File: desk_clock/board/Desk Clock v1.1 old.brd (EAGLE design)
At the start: 79 x 35.9 mm, 17 parts, among them IC1 PIC16F628P, IC2 MAX7219CNG, U1 TMP75D

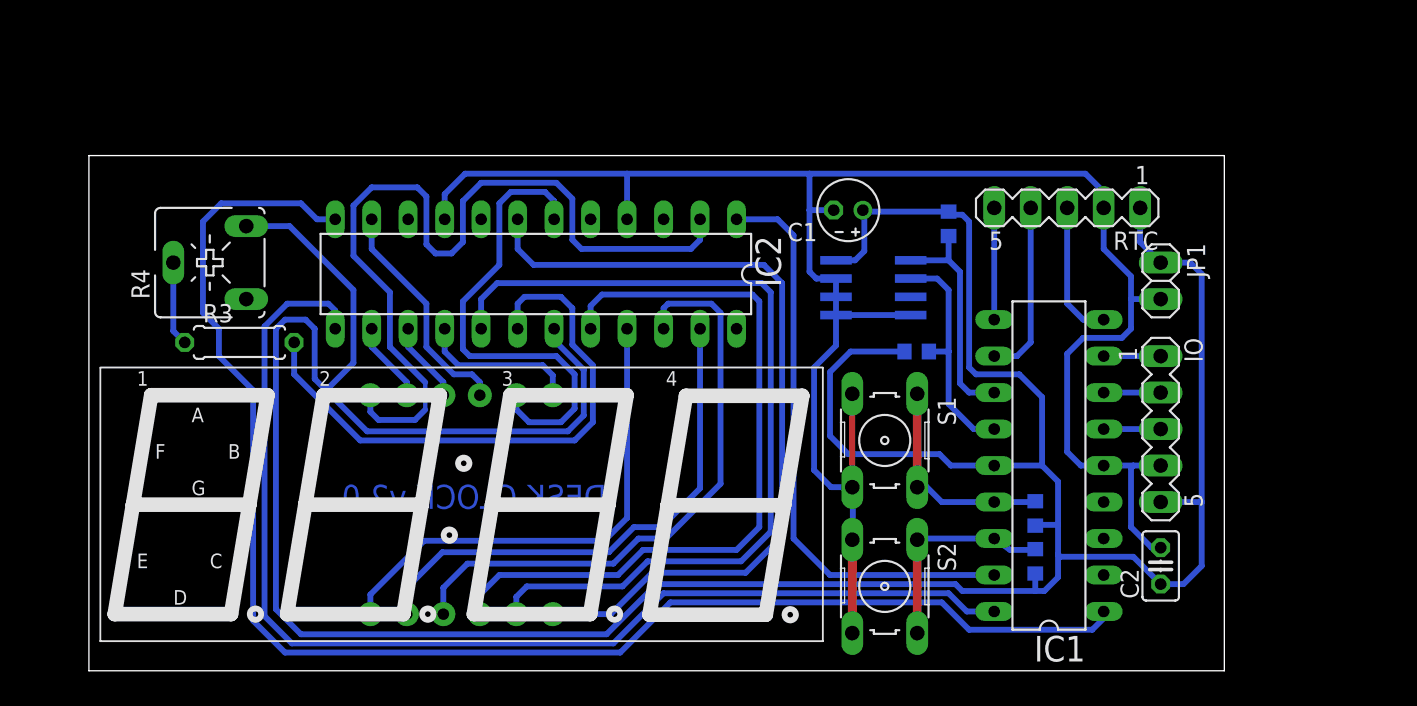
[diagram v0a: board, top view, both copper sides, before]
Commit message: Hw revision 2.0 (compact board). Firmware updated to reflect that. Several small modifications made for better behavior.
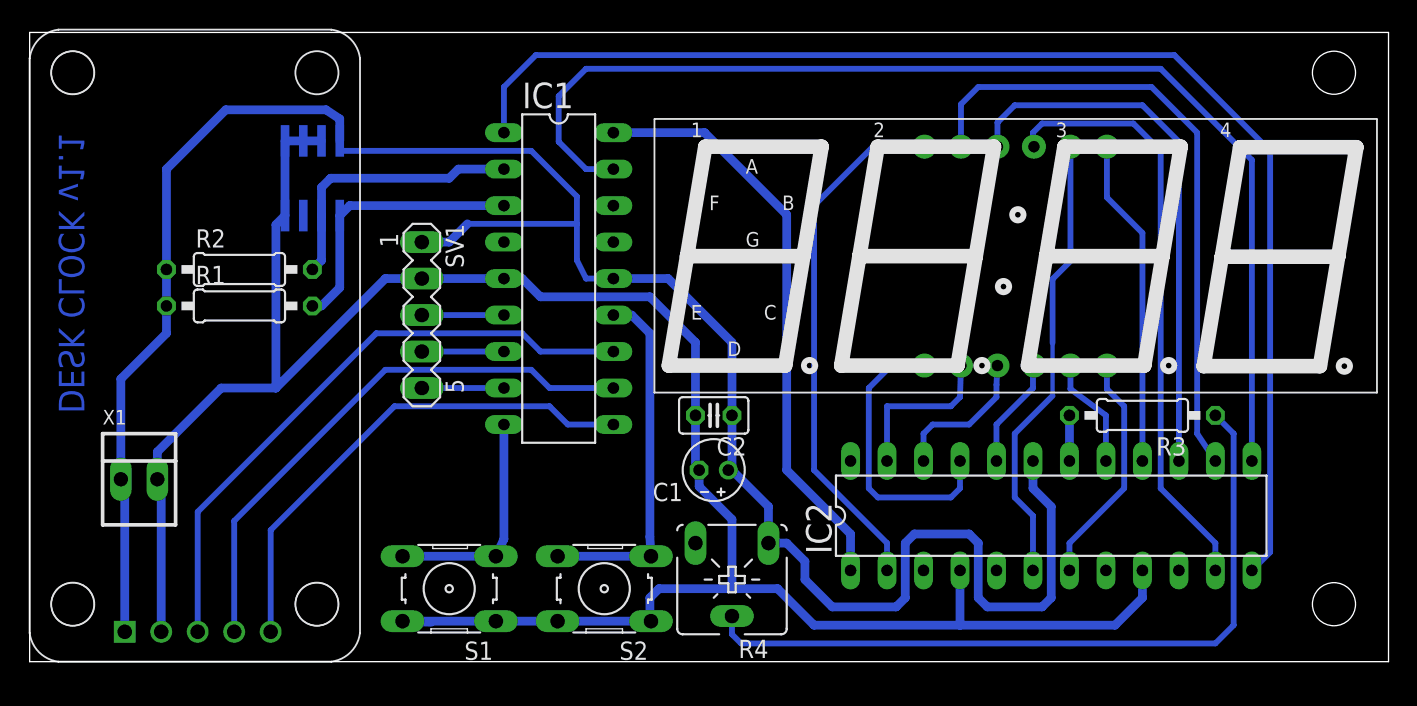
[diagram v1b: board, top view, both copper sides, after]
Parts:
- removed IO, RTC: (no value), con-lstb:MA05-1
- removed JP1: (no value), pinhead:1X02
- removed R5, R6: 10K, resistor:R0603
- added SV1: (no value), con-lstb:MA05-1
- added U$2: DS1302_BOARD, DS1302_board:DS1302_BOARD
- added X1: 22-23-2021, con-molex:22-23-2021
- R1, R2: device resistor:R0603 -> resistor:0207/10
- R3: device resistor:0207/7 -> resistor:0207/10
- R4: value (none) -> 100K
- moved R3 63.1 mm to (77.5, 17.8), turned to 180 degrees
- moved R1 49.7 mm to (14.6, 25.4), flipped to the top, turned to 0 degrees
- moved R2 47.5 mm to (14.6, 27.9), flipped to the top, turned to 0 degrees
- moved R4 42.5 mm to (48.9, 6.35), turned to 180 degrees
- moved U$1 42.3 mm to (43.5, 19.4)
- moved U1 39.8 mm to (19.7, 34.3), turned to 0 degrees
- moved IC2 39.6 mm to (71.1, 10.8), turned to 0 degrees
- moved IC1 36.5 mm to (36.8, 27.3), turned to 270 degrees
- moved C2 32.8 mm to (47.6, 17.8), turned to 180 degrees
- moved S1 32.0 mm to (29.2, 5.71), turned to 180 degrees
- moved C1 20.4 mm to (47.6, 14.0)
- moved S2 19.5 mm to (40.0, 5.71), turned to 180 degrees
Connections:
- net MAX_LD renamed N$22
- removed net $N18: IC1.15, R5.2, S1.1, S1.2
- removed net $N9: IC1.16, R6.2, S2.1, S2.2
- removed net INT: IC1.6, IO.3
- removed net MAX_CLK: IC1.18, IC2.13
- removed net MAX_DIN: IC1.17, IC2.1
- new net N$18: IC1.6, SV1.3
- new net N$19: IC1.17, IC2.13
- new net N$20: IC1.13, S2.3, S2.4
- new net N$21: IC1.18, IC2.1
- new net N$9: IC1.9, S1.3, S1.4
- net DS_CLK: now also IC1.12, U$2.CLK; no longer IC1.9, RTC.3
- net DS_DAT: now also U$2.DAT; no longer RTC.4
- net DS_RST: now also U$2.RST; no longer RTC.5
- net GND: now also S1.1, S1.2, S2.1, S2.2, SV1.2, U$2.GND, X1.2; no longer IO.4, JP1.2, RTC.2, S1.3, S1.4, S2.3, S2.4
- net N$16: now also SV1.5; no longer IO.1
- net N$17: now also SV1.4; no longer IO.2
- net SCL: now also IC1.2; no longer IC1.13
- net SDA: now also IC1.3; no longer IC1.12
- net VDD: now also R4.A, SV1.1, U$2.VDD, X1.1; no longer IO.5, JP1.1, R4.E, R5.1, R6.1, RTC.1
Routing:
- net VDD: track 241.4 -> 154.8 mm
- net MAX_CLK: track 80.8 -> 0.00 mm
- net N$19: track 0.00 -> 80.4 mm
- net N$5: track 60.4 -> 7.89 mm
- net N$15: track 5.89 -> 52.1 mm
- net N$11: track 52.3 -> 7.72 mm
- net N$21: track 0.00 -> 41.0 mm
- net N$6: track 57.3 -> 16.3 mm
- net MAX_DIN: track 40.6 -> 0.00 mm
- net N$7: track 5.64 -> 44.5 mm
- net N$14: track 40.1 -> 3.18 mm
- net DS_CLK: track 9.67 -> 43.0 mm
- net N$8: track 5.64 -> 38.1 mm
- net N$4: track 41.8 -> 10.2 mm
- net DS_RST: track 7.78 -> 35.0 mm
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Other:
- board size 79 x 35.9 mm -> 94.6 x 43.8 mm
- board text added: "DESK CLOCK v1.1"
- board text removed: "DESK CLOCK v2.0"
